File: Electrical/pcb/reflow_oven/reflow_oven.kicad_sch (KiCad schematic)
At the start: 0 parts

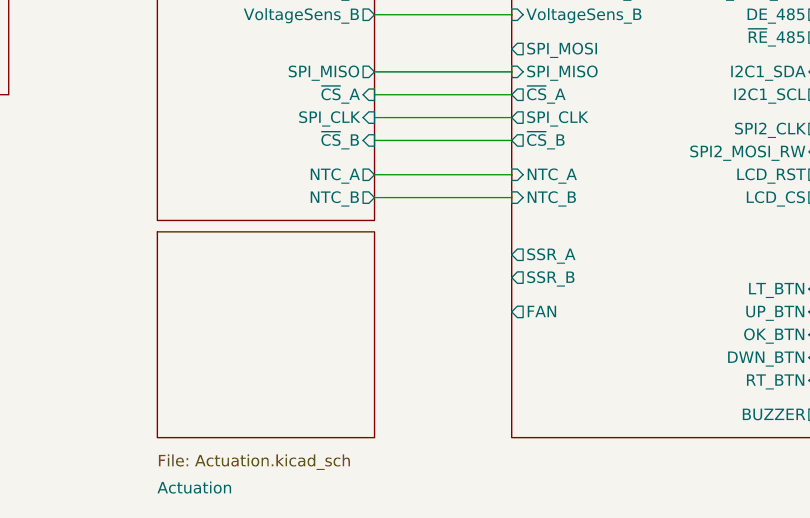
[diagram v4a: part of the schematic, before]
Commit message: functionality
done output stage
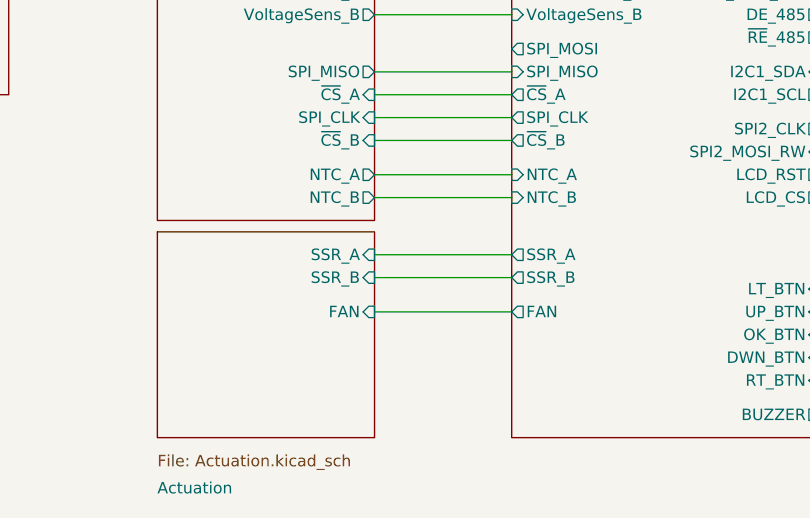
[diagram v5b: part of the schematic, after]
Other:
- sheet Actuation ports: added FAN, SSR_A, SSR_B; removed none
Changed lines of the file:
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@@
     (rev "1.0")
   )
+  (wire (pts (xy 137.16 105.41) (xy 152.4 105.41))
+    (stroke (width 0) (type default) (color 0 0 0 0))
+  )
   (wire (pts (xy 137.16 71.12) (xy 152.4 71.12))
     (stroke (width 0) (type default) (color 0 0 0 0))
@@
     (stroke (width 0) (type default) (color 0 0 0 0))
   )
+  (wire (pts (xy 137.16 102.87) (xy 152.4 102.87))
+    (stroke (width 0) (type default) (color 0 0 0 0))
+  )
   (wire (pts (xy 137.16 82.55) (xy 152.4 82.55))
     (stroke (width 0) (type default) (color 0 0 0 0))
@@
   )
   (wire (pts (xy 137.16 90.17) (xy 152.4 90.17))
+    (stroke (width 0) (type default) (color 0 0 0 0))
+  )
+  (wire (pts (xy 137.16 109.22) (xy 152.4 109.22))
     (stroke (width 0) (type default) (color 0 0 0 0))
   )
@@
     (property "Sheet file" "Actuation.kicad_sch" (id 1) (at 113.03 125.0446 0)
       (effects (font (size 1.27 1.27)) (justify left top))
+    )
+    (pin "SSR_B" input (at 137.16 105.41 0)
+      (effects (font (size 1.27 1.27)) (justify right))
+    )
+    (pin "SSR_A" input (at 137.16 102.87 0)
+      (effects (font (size 1.27 1.27)) (justify right))
+    )
+    (pin "FAN" input (at 137.16 109.22 0)
+      (effects (font (size 1.27 1.27)) (justify right))
     )
   )
@@
       (reference "#PWR0118") (unit 1) (value "GNDA") (footprint "")
     )
+    (path "/e529b68e-658c-449e-b839-b72d069f9257/520fd2fa-2842-4f5d-b056-60d11cca94c8"
+      (reference "#PWR0119") (unit 1) (value "+5V") (footprint "")
+    )
+    (path "/e529b68e-658c-449e-b839-b72d069f9257/d79596c3-b986-4838-80bd-a1949505881c"
+      (reference "#PWR0120") (unit 1) (value "+3V3") (footprint "")
+    )
+    (path "/e529b68e-658c-449e-b839-b72d069f9257/51bac7c5-508b-4a62-8a70-5e222a436032"
+      (reference "#PWR0121") (unit 1) (value "+5V") (footprint "")
+    )
+    (path "/e529b68e-658c-449e-b839-b72d069f9257/780f0c9d-1b9f-4994-98a3-9f841dbcf647"
+      (reference "#PWR0122") (unit 1) (value "GND") (footprint "")
+    )
+    (path "/e529b68e-658c-449e-b839-b72d069f9257/816221aa-ce89-41ea-949e-4d513901e70f"
+      (reference "#PWR0123") (unit 1) (value "GND") (footprint "")
+    )
+    (path "/a4495d77-238e-40f1-9ffb-145d8b1cecb5/dcffe0bc-5b66-4983-be00-f613378f4aba"
+      (reference "#PWR0124") (unit 1) (value "+5V") (footprint "")
+    )
+    (path "/a4495d77-238e-40f1-9ffb-145d8b1cecb5/2ebb764a-7a27-4f53-a328-af14434858e8"
+      (reference "#PWR0125") (unit 1) (value "GND") (footprint "")
+    )
+    (path "/a4495d77-238e-40f1-9ffb-145d8b1cecb5/55621626-109b-4224-9083-305fc916a578"
+      (reference "#PWR0126") (unit 1) (value "GND") (footprint "")
+    )
+    (path "/a4495d77-238e-40f1-9ffb-145d8b1cecb5/6a999289-cd0f-4397-bc41-d73e60d3791b"
+      (reference "#PWR0127") (unit 1) (value "GND") (footprint "")
+    )
+    (path "/a4495d77-238e-40f1-9ffb-145d8b1cecb5/315ca881-3bd1-4c17-b048-6e30776e0088"
+      (reference "#PWR0128") (unit 1) (value "+5V") (footprint "")
+    )
+    (path "/a4495d77-238e-40f1-9ffb-145d8b1cecb5/444e22fa-7b5b-4684-94b0-c51ffc3f2afe"
+      (reference "#PWR0129") (unit 1) (value "GND") (footprint "")
+    )
     (path "/e529b68e-658c-449e-b839-b72d069f9257/0032ab92-3d2c-4df8-b4c4-beb277ac11bb"
       (reference "C1") (unit 1) (value "C") (footprint "footprint_lib:MXH104K305E10")
@@
       (reference "C37") (unit 1) (value "100nF") (footprint "Capacitor_SMD:C_0603_1608Metric")
     )
+    (path "/a4495d77-238e-40f1-9ffb-145d8b1cecb5/512a83bc-9fb0-4490-8646-0d0cda310aa6"
+      (reference "C38") (unit 1) (value "100nF") (footprint "Capacitor_SMD:C_0603_1608Metric")
+    )
+    (path "/a4495d77-238e-40f1-9ffb-145d8b1cecb5/1f71ba16-4f2b-43d1-ac1a-502192a89b53"
+      (reference "C39") (unit 1) (value "100nF") (footprint "Capacitor_SMD:C_0603_1608Metric")
+    )
     (path "/e529b68e-658c-449e-b839-b72d069f9257/513f0394-5f68-402c-967a-6019783434be"
       (reference "D1") (unit 1) (value "DSS34") (footprint "Diode_SMD:D_SOD-123F")
@@
       (reference "D13") (unit 1) (value "BAT54S") (footprint "Package_TO_SOT_SMD:SOT-23")
     )
+    (path "/e529b68e-658c-449e-b839-b72d069f9257/19104c48-71f9-46cb-a01d-54d9b4e25a70"
+      (reference "D14") (unit 1) (value "DSS34") (footprint "Diode_SMD:D_SOD-123F")
+    )
+    (path "/e529b68e-658c-449e-b839-b72d069f9257/e4825afd-2c1e-44d7-9612-a52ab7b4d02a"
+      (reference "D15") (unit 1) (value "DSS34") (footprint "Diode_SMD:D_SOD-123F")
+    )
+    (path "/a4495d77-238e-40f1-9ffb-145d8b1cecb5/8e026688-5571-487b-94ed-82bb53331610"
+      (reference "D16") (unit 1) (value "LED") (footprint "LED_SMD:LED_0603_1608Metric")
+    )
+    (path "/a4495d77-238e-40f1-9ffb-145d8b1cecb5/6785c683-d243-497b-8439-89f24d7b0c05"
+      (reference "D17") (unit 1) (value "LED") (footprint "LED_SMD:LED_0603_1608Metric")
+    )
     (path "/e529b68e-658c-449e-b839-b72d069f9257/c7baae09-cf3e-4c79-bc1f-39f91f3a5580"
       (reference "F1") (unit 1) (value "fuse_holder") (footprint "footprint_lib:64600001223")
@@
       (reference "J13") (unit 1) (value "NTC_B IN") (footprint "TerminalBlock_Phoenix:TerminalBlock_Phoenix_MPT-0,5-2-2.54_1x02_P2.54mm_Horizontal")
     )
+    (path "/e529b68e-658c-449e-b839-b72d069f9257/5accfe66-1f24-4c7c-b7f7-c2126b84768c"
+      (reference "J14") (unit 1) (value "3V3 out") (footprint "TerminalBlock_Phoenix:TerminalBlock_Phoenix_MPT-0,5-2-2.54_1x02_P2.54mm_Horizontal")
+    )
+    (path "/e529b68e-658c-449e-b839-b72d069f9257/ba87e874-b4fe-4507-b77c-aae69e135376"
+      (reference "J15") (unit 1) (value "5V out") (footprint "TerminalBlock_Phoenix:TerminalBlock_Phoenix_MPT-0,5-2-2.54_1x02_P2.54mm_Horizontal")
+    )
+    (path "/a4495d77-238e-40f1-9ffb-145d8b1cecb5/231e134b-1d52-49cf-953d-2de99c90b1e5"
+      (reference "J16") (unit 1) (value "SSR_A") (footprint "TerminalBlock_Phoenix:TerminalBlock_Phoenix_MPT-0,5-2-2.54_1x02_P2.54mm_Horizontal")
+    )
+    (path "/a4495d77-238e-40f1-9ffb-145d8b1cecb5/6a372e3f-8119-48db-80d5-ceb4e83dee18"
+      (reference "J17") (unit 1) (value "FAN power in") (footprint "TerminalBlock_Phoenix:TerminalBlock_Phoenix_MPT-0,5-2-2.54_1x02_P2.54mm_Horizontal")
+    )
+    (path "/a4495d77-238e-40f1-9ffb-145d8b1cecb5/7c2188b9-8d69-45f5-9056-8e2a1dbb6e84"
+      (reference "J18") (unit 1) (value "FAN out") (footprint "TerminalBlock_Phoenix:TerminalBlock_Phoenix_MPT-0,5-2-2.54_1x02_P2.54mm_Horizontal")
+    )
+    (path "/a4495d77-238e-40f1-9ffb-145d8b1cecb5/f1d6fb14-d2c9-4a8b-8c9c-7041ad785288"
+      (reference "J19") (unit 1) (value "SSR_B") (footprint "TerminalBlock_Phoenix:TerminalBlock_Phoenix_MPT-0,5-2-2.54_1x02_P2.54mm_Horizontal")
+    )
     (path "/53a208f1-6323-4fa9-b554-8d00eaeb3dc8/d747d681-eb34-4579-9ae1-c53de03bea57"
       (reference "JP1") (unit 1) (value "boot") (footprint "Jumper:SolderJumper-2_P1.3mm_Open_RoundedPad1.0x1.5mm")
     )
+    (path "/a4495d77-238e-40f1-9ffb-145d8b1cecb5/12fac911-a693-46ce-83f9-6918f18a39c3"
+      (reference "JP2") (unit 1) (value "SolderJumper_2_Open") (footprint "Jumper:SolderJumper-2_P1.3mm_Open_RoundedPad1.0x1.5mm")
+    )
     (path "/53a208f1-6323-4fa9-b554-8d00eaeb3dc8/b9e66a0b-a2bc-42bd-b165-c75f315fb9a7"
       (reference "N1") (unit 1) (value "Net-Tie_2") (footprint "NetTie:NetTie-2_SMD_Pad2.0mm")
@@
       (reference "P1") (unit 1) (value "USB_C_Receptacle_USB2.0") (footprint "Connector_USB:USB_C_Receptacle_Palconn_UTC16-G")
     )
+    (path "/a4495d77-238e-40f1-9ffb-145d8b1cecb5/45a7c1cd-f274-44d5-9b72-eb919b1e812f"
+      (reference "Q1") (unit 1) (value "DMN13H750S") (footprint "Package_TO_SOT_SMD:SOT-23")
+    )
+    (path "/a4495d77-238e-40f1-9ffb-145d8b1cecb5/96d1968a-b38b-464b-b2dd-f53595d3970b"
+      (reference "Q2") (unit 1) (value "AO3402") (footprint "Package_TO_SOT_SMD:SOT-23")
+    )
+    (path "/a4495d77-238e-40f1-9ffb-145d8b1cecb5/65cd5e02-77cd-4411-ab49-2eda26fa9114"
+      (reference "Q3") (unit 1) (value "DMN13H750S") (footprint "Package_TO_SOT_SMD:SOT-23")
+    )
     (path "/e529b68e-658c-449e-b839-b72d069f9257/7d02854a-b95e-479e-9a39-ae1d17969225"
       (reference "R1") (unit 1) (value "1k") (footprint "Resistor_SMD:R_0603_1608Metric")
@@
       (reference "R66") (unit 1) (value "100K") (footprint "Resistor_SMD:R_0603_1608Metric")
     )
+    (path "/a4495d77-238e-40f1-9ffb-145d8b1cecb5/85d8578b-e479-4ca3-b0f5-e54237645320"
+      (reference "R67") (unit 1) (value "100") (footprint "Resistor_SMD:R_0603_1608Metric")
+    )
+    (path "/a4495d77-238e-40f1-9ffb-145d8b1cecb5/0f528f95-57af-4878-be94-9c6446447665"
+      (reference "R68") (unit 1) (value "100k") (footprint "Resistor_SMD:R_0603_1608Metric")
+    )
+    (path "/a4495d77-238e-40f1-9ffb-145d8b1cecb5/7945271e-60a0-4e73-ab12-4dd11db29647"
+      (reference "R69") (unit 1) (value "100") (footprint "Resistor_SMD:R_0603_1608Metric")
+    )
+    (path "/a4495d77-238e-40f1-9ffb-145d8b1cecb5/daa716f4-431d-4012-b2ee-88d5814798f5"
+      (reference "R70") (unit 1) (value "100k") (footprint "Resistor_SMD:R_0603_1608Metric")
+    )
+    (path "/a4495d77-238e-40f1-9ffb-145d8b1cecb5/fd353c85-a209-4dc5-824c-449a16ed8cff"
+      (reference "R71") (unit 1) (value "1k") (footprint "Resistor_SMD:R_0603_1608Metric")
+    )
+    (path "/a4495d77-238e-40f1-9ffb-145d8b1cecb5/376d4ef3-6b4c-4124-b698-99a07da805da"
+      (reference "R72") (unit 1) (value "10K") (footprint "Resistor_SMD:R_0603_1608Metric")
+    )
+    (path "/a4495d77-238e-40f1-9ffb-145d8b1cecb5/477d02b3-55c1-4dce-b596-59cfd71a2485"
+      (reference "R73") (unit 1) (value "100") (footprint "Resistor_SMD:R_0603_1608Metric")
+    )
+    (path "/a4495d77-238e-40f1-9ffb-145d8b1cecb5/fe67cdb5-c38d-4c70-8e8d-292fff638338"
+      (reference "R74") (unit 1) (value "100k") (footprint "Resistor_SMD:R_0603_1608Metric")
+    )
+    (path "/a4495d77-238e-40f1-9ffb-145d8b1cecb5/98210c00-9a0b-4aa8-a55f-5b9657763d07"
+      (reference "R75") (unit 1) (value "1k") (footprint "Resistor_SMD:R_0603_1608Metric")
+    )
     (path "/e529b68e-658c-449e-b839-b72d069f9257/5c5583d6-ae8a-4491-81cc-046920b3a447"
